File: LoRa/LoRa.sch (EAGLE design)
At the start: 9 parts, among them IC1 FT232RL, J1 UP2-AH-1-TH, U1 RFM69HCW, U3 AP2112K-3.3, X1 uFL/SMA

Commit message: Stuff
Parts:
- removed IC1: FT232RL, ftdichip:FT232RL
- added C10, C11: 20pF, SparkFun-Capacitors:4.7UF0603
- added C3, C5, C7: 1.0uF, SparkFun-Capacitors:1.0UF-0603-16V-10%
- added C4, C6: 0.1uF, SparkFun-Capacitors:0.1UF-0603-25V-(+80/-20%)
- added C8: 22uF, microbuilder:CAP_CERAMIC0805-NOOUTLINE
- added C9: 10uF, microbuilder:CAP_CERAMIC0805-NOOUTLINE
- added L1: 2.2uH/NRH2412T2R2MNGH, microbuilder:INDUCTORNRH2412T
- added R2, R3, R4, R6: 10k, SparkFun-Resistors:1KOHM-0603-1/10W-1%
- added SV2: (no value), con-lsta:FE05-1
- added U2: RFM69HCW, microbuilder:RFM69HCW_SMT
- added U4: BSS138, BSS138:BSS138
- added U5: LM3671MF-3.3/NOPB, microbuilder:VREG_LM3671
- added Y1: ECS-80-S-4X, ECS-80-S-4X:ECS-80-S-4X
- C1: value 10uF -> 0.1uF; device SparkFun-Capacitors:10UF-0603-6.3V-20% -> SparkFun-Capacitors:0.1UF-0603-25V-(+80/-20%)
- U1: value RFM69HCW -> STM32L053C8T6; device microbuilder:RFM69HCW_SMT -> STM32L053C8T6:STM32L053C8T6
- U3: value AP2112K-3.3 -> BSS138; device microbuilder:VREG_SOT23-5 -> BSS138:BSS138
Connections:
- removed net D_MINUS: J1.2
- removed net D_PLUS: J1.3
- removed net MISO: U1.MISO
- removed net MOSI: U1.MOSI
- removed net SCK: U1.SCK
- removed net VIN: C1.1, J1.1, R1.1, U3.IN
- new net 5V: C9.1, J1.1, R1.1, R3.1, R6.1, U5.VIN
- new net EN: R1.2, U5.EN
- new net NRST: SV2.1, U1.NRST
- new net OSC_IN: C11.1, U1.PH0-OSC_IN, Y1.2
- new net OSC_OUT: C10.1, U1.PH1-OSC_OUT, Y1.1
- new net SPI1_MISO: U1.PA6, U2.MISO
- new net SPI1_MOSI: U2.MOSI
- new net SPI1_SCK: U1.PA5, U2.SCK
- new net SPI_MOSI: U1.PA7
- new net SWCLK: SV2.4, U1.PA14
- new net SWDIO: SV2.2, U1.PA13
- new net USB_DM_3V3: R4.1, U1.PA11, U4.S
- new net USB_DM_5V: J1.2, R6.2, U4.D
- new net USB_DP_3V3: R2.1, U1.PA12, U3.S
- new net USB_DP_5V: J1.3, R3.2, U3.D
- net 3.3V: now also C1.1, C3.1, C4.1, C5.1, C6.1, C7.1, C8.1, L1.2, R2.2, R4.2, SV2.5, U1.VDDA, U1.VDD_USB, U2.VDD, U3.G, U4.G, U5.FB; no longer U3.OUT
- net CS: now also U2.NSS; no longer U1.NSS
- net DIO0: now also U2.DIO0; no longer U1.DIO0
- net DIO1: now also U2.DIO1; no longer U1.DIO1
- net DIO2: now also U2.DIO2; no longer U1.DIO2
- net DIO3: now also U2.DIO3; no longer U1.DIO3
- net DIO4: now also U2.DIO4; no longer U1.DIO4
- net DIO5: now also U2.DIO5; no longer U1.DIO5
- net GND: now also C10.2, C11.2, C3.2, C4.2, C5.2, C6.2, C7.2, C8.2, C9.2, SV2.3, U1.VSS, U1.VSSA, U2.GND@1, U2.GND@2, U2.GND@3, U5.GND; no longer U1.GND@1, U1.GND@2, U1.GND@3, U3.GND
- net N$1: now also U2.ANT; no longer U1.ANT
- net N$2: now also L1.1, U5.SW; no longer R1.2, U3.EN
- net RST: now also U2.RESET; no longer U1.RESET
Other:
- note added: "OSCILLATOR"
- note removed: "Linear Regulator"

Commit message: updates
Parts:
- added C12: UWD0J560MCL1GS, 56uF_Cap_6.3v:UWD0J560MCL1GS
- added C13, C16: 1.0uF, SparkFun-Capacitors:1.0UF-0603-16V-10%
- added C14, C15: 0.1uF, SparkFun-Capacitors:0.1UF-0603-25V-(+80/-20%)
- added C17: 4.7uF, SparkFun-Capacitors:4.7UF0603
- added R5: 1k, SparkFun-Resistors:1KOHM-0603-1/10W-1%
- added RESET: SWITCH, DiscreteComponents:SWITCH
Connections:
- new net +3V3: R5.2
- net 3.3V: now also C12.1, C13.1, C14.1, C15.1, C16.1
- net CS: now also U1.PA4
- net DIO0: now also U1.PB1
- net GND: now also C12.2, C13.2, C14.2, C15.2, C16.2, C17.2, RESET.P$1
- net NRST: now also C17.1, R5.1, RESET.P$2
- net RST: now also U1.PB0
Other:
- moved on the sheet: C1, C3, J1

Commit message: Finished Initial Routing
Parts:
- removed R2, R3, R4, R6: 10k, SparkFun-Resistors:1KOHM-0603-1/10W-1%
- removed U3, U4: BSS138, BSS138:BSS138
- added C18: 0.1uF, SparkFun-Capacitors:0.1UF-0603-25V-(+80/-20%)
- added CR1: USBLC6-2SC6, ESD_Protection:USBLC6-2SC6
- added J2, J3: (no value), SparkFun-Connectors:CONN_03
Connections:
- removed net +3V3: R5.2
- removed net SPI_MOSI: U1.PA7
- removed net USB_DM_5V: J1.2, R6.2, U4.D
- removed net USB_DP_5V: J1.3, R3.2, U3.D
- new net USB_DM: CR1.I/O2, J1.2
- new net USB_DP: CR1.I/O1, J1.3
- net 3.3V: now also C18.1, CR1.VBUS, J3.1, J3.2, J3.3, R5.2; no longer R2.2, R4.2, U3.G, U4.G
- net 5V: no longer R3.1, R6.1
- net GND: now also C18.2, CR1.GND, J2.1, J2.2, J2.3
- net SPI1_MOSI: now also U1.PA7
- net USB_DM_3V3: now also CR1.I/O2_2; no longer R4.1, U4.S
- net USB_DP_3V3: now also CR1.I/O1_2; no longer R2.1, U3.S
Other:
- note added: "ESD Protection"

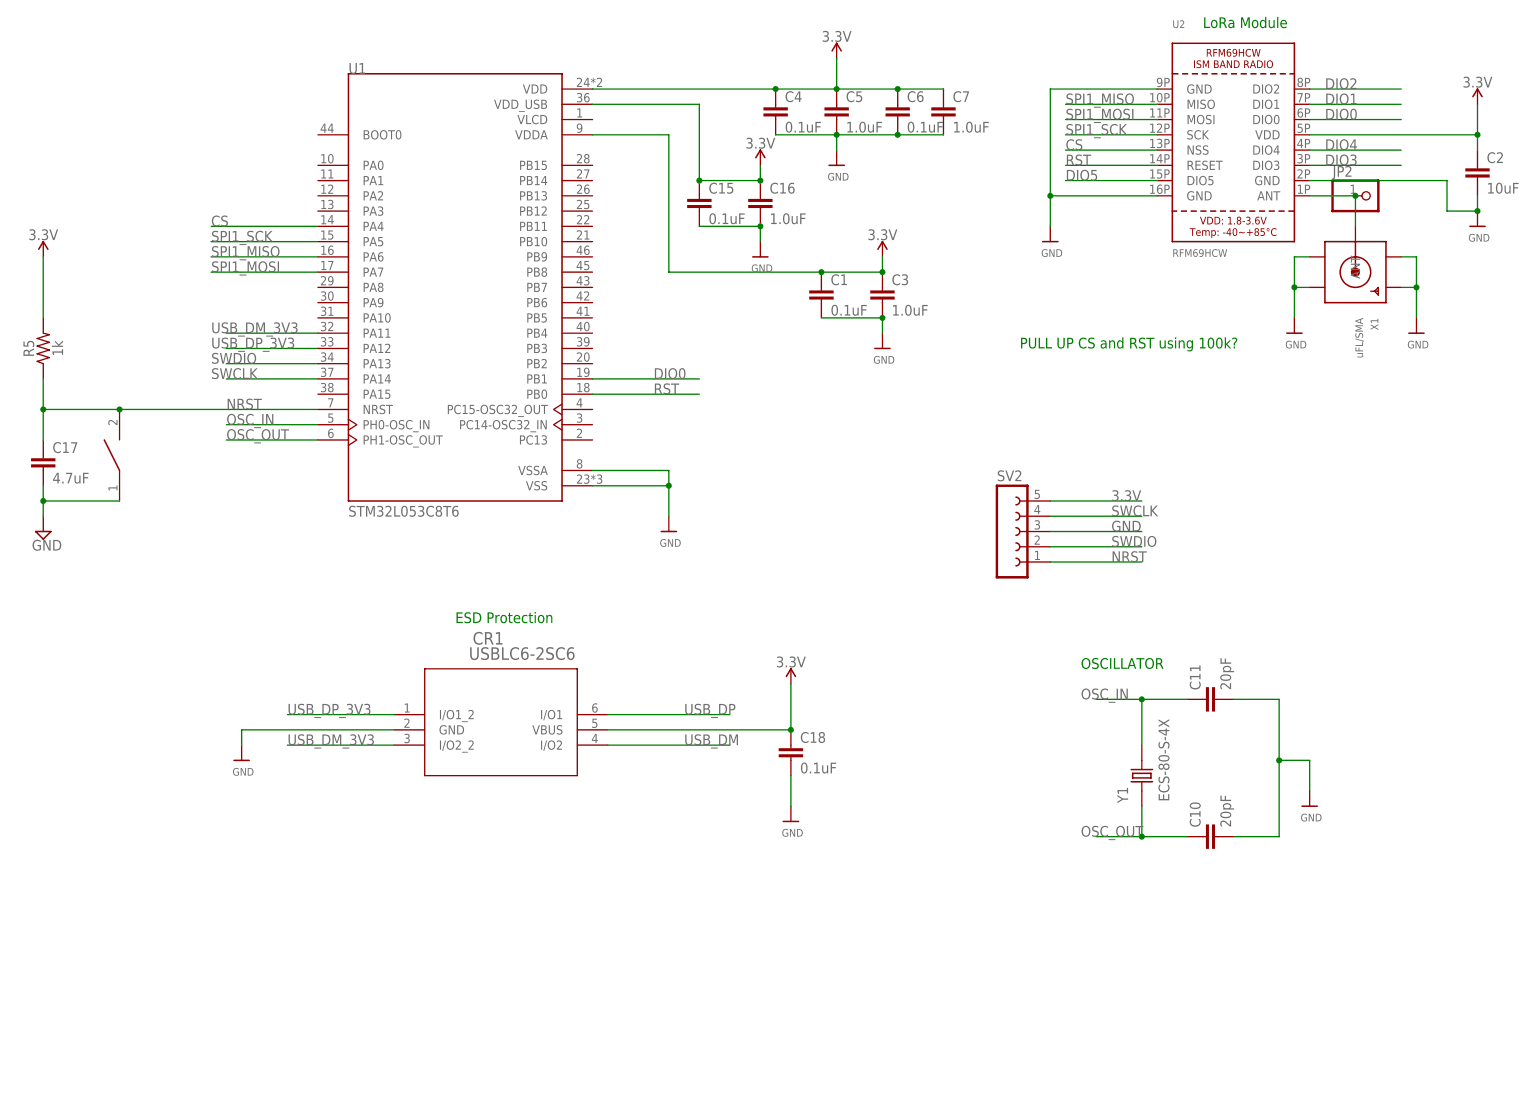
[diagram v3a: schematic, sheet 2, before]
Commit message: Added Labels to Schematic
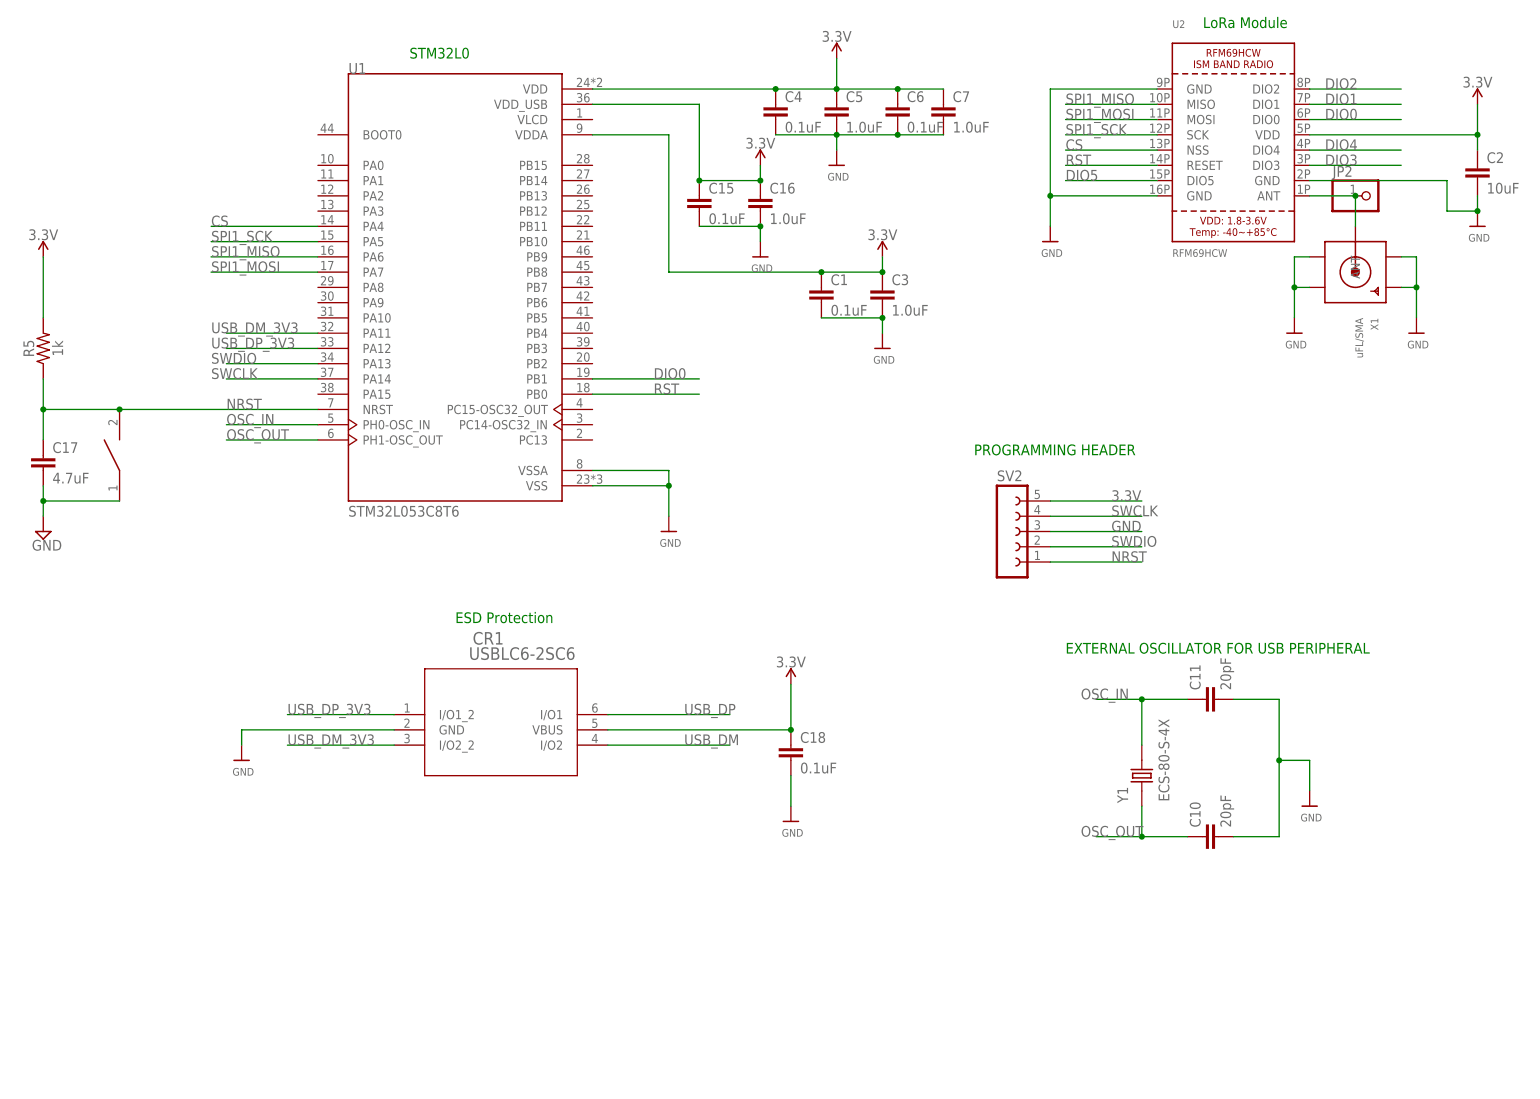
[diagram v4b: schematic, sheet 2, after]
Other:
- note added: "BUCK CONVERTER"
- note added: "CAPACITOR NETWORK FOR BUCK CONVERTER OUTPUT"
- note added: "EXTERNAL OSCILLATOR FOR USB PERIPHERAL"
- note added: "PROGRAMMING HEADER"
- note added: "STAR GROUND HEADERS"
- note added: "STM32L0"
- note added: "USB MALE CONNECTOR"
- note removed: "OSCILLATOR"
- note removed: "PULL UP CS and RST using 100k?"
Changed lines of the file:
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@@
 <sheets>
 <sheet>
-<description>Power and FTDI</description>
+<description>Power</description>
 <plain>
+<text x="55.88" y="218.44" size="1.778" layer="91">BUCK CONVERTER</text>
+<text x="142.24" y="210.82" size="1.778" layer="91">USB MALE CONNECTOR</text>
+<text x="48.26" y="165.1" size="1.778" layer="91">CAPACITOR NETWORK FOR BUCK CONVERTER OUTPUT</text>
+<text x="147.32" y="165.1" size="1.778" layer="91">STAR GROUND HEADERS</text>
 </plain>
 <instances>
@@
 <plain>
 <text x="205.74" y="228.6" size="1.778" layer="91">LoRa Module</text>
-<text x="175.26" y="175.26" size="1.778" layer="91">PULL UP CS and RST using 100k?</text>
-<text x="185.42" y="121.92" size="1.778" layer="91">OSCILLATOR</text>
+<text x="182.88" y="124.46" size="1.778" layer="91">EXTERNAL OSCILLATOR FOR USB PERIPHERAL</text>
 <text x="81.28" y="129.54" size="1.778" layer="91">ESD Protection</text>
+<text x="167.64" y="157.48" size="1.778" layer="91">PROGRAMMING HEADER</text>
+<text x="73.66" y="223.52" size="1.778" layer="91">STM32L0</text>
 </plain>
 <instances>

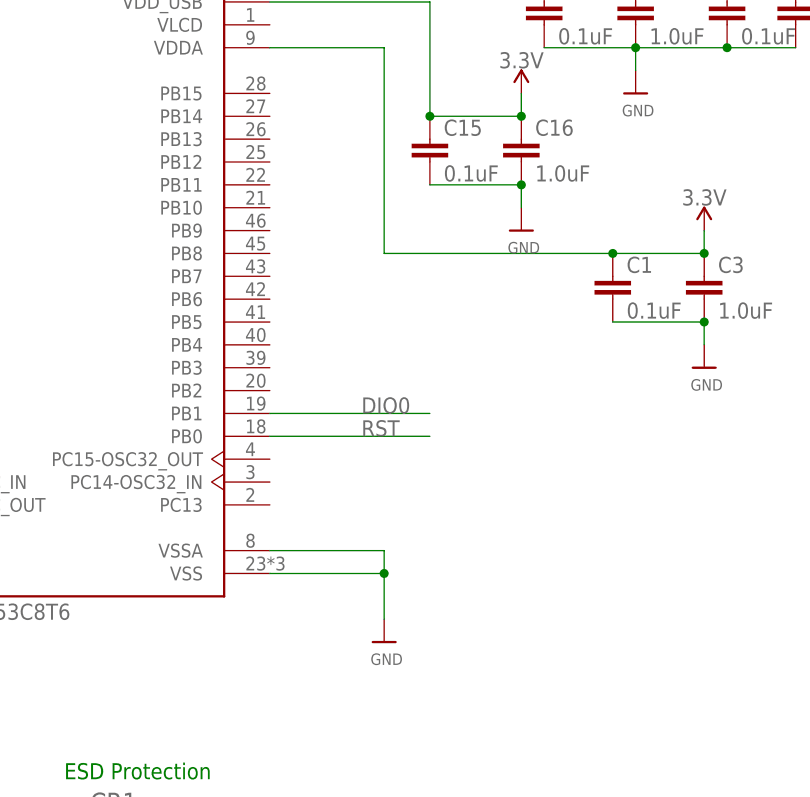
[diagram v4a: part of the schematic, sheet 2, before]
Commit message: added led indicator
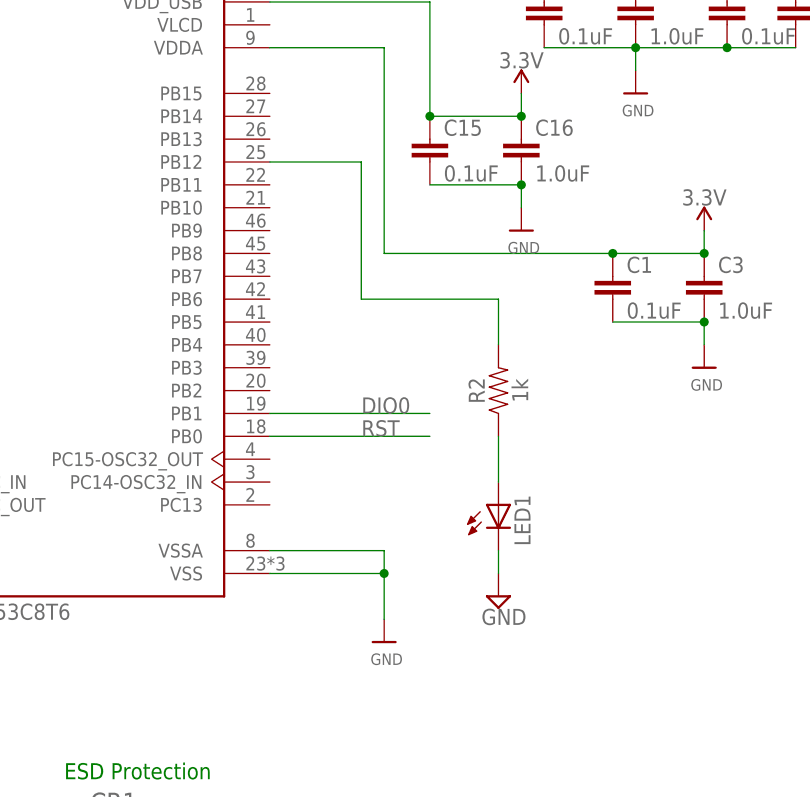
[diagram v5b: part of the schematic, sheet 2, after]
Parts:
- added LED1: (no value), led:LEDCHIP-LED0805
- added R2: 1k, SparkFun-Resistors:1KOHM-0603-1/10W-1%
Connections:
- new net N$3: R2.2, U1.PB12
- new net N$4: LED1.A, R2.1
- net GND: now also LED1.C
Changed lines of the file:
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@@
 <part name="J3" library="SparkFun-Connectors" library_urn="urn:adsk.eagle:library:513" deviceset="CONN_03" device="" package3d_urn="urn:adsk.eagle:package:38063/1"/>
 <part name="SUPPLY6" library="SparkFun-PowerSymbols" library_urn="urn:adsk.eagle:library:530" deviceset="3.3V" device=""/>
+<part name="LED1" library="led" library_urn="urn:adsk.eagle:library:259" deviceset="LED" device="CHIP-LED0805" package3d_urn="urn:adsk.eagle:package:15818/2">
+<attribute name="SPICEPREFIX" value="L"/>
+</part>
+<part name="GND1" library="supply2" library_urn="urn:adsk.eagle:library:372" deviceset="GND" device=""/>
+<part name="R2" library="SparkFun-Resistors" library_urn="urn:adsk.eagle:library:532" deviceset="1KOHM" device="-0603-1/10W-1%" package3d_urn="urn:adsk.eagle:package:39650/1" value="1k"/>
 </parts>
 <sheets>
@@
 <instance part="U$16" gate="G$1" x="45.72" y="106.68"/>
 <instance part="SUPPLY6" gate="G$1" x="12.7" y="190.5"/>
+<instance part="LED1" gate="G$1" x="129.54" y="160.02"/>
+<instance part="GND1" gate="GND" x="129.54" y="149.86">
+<attribute name="VALUE" x="127.635" y="146.685" size="1.778" layer="96"/>
+</instance>
+<instance part="R2" gate="G$1" x="129.54" y="172.72" rot="R90">
+<attribute name="NAME" x="128.016" y="172.72" size="1.778" layer="95" font="vector" rot="R90" align="bottom-center"/>
+<attribute name="VALUE" x="131.064" y="172.72" size="1.778" layer="96" font="vector" rot="R90" align="top-center"/>
+</instance>
 </instances>
 <busses>
@@
 <wire x1="71.12" y1="111.76" x2="45.72" y2="111.76" width="0.1524" layer="91"/>
 <wire x1="45.72" y1="111.76" x2="45.72" y2="109.22" width="0.1524" layer="91"/>
+</segment>
+<segment>
+<pinref part="LED1" gate="G$1" pin="C"/>
+<pinref part="GND1" gate="GND" pin="GND"/>
+<wire x1="129.54" y1="154.94" x2="129.54" y2="152.4" width="0.1524" layer="91"/>
 </segment>
 </net>
@@
 </segment>
 </net>
+<net name="N$3" class="0">
+<segment>
+<pinref part="U1" gate="G$1" pin="PB12"/>
+<wire x1="104.14" y1="198.12" x2="114.3" y2="198.12" width="0.1524" layer="91"/>
+<wire x1="114.3" y1="198.12" x2="114.3" y2="182.88" width="0.1524" layer="91"/>
+<wire x1="114.3" y1="182.88" x2="129.54" y2="182.88" width="0.1524" layer="91"/>
+<pinref part="R2" gate="G$1" pin="2"/>
+<wire x1="129.54" y1="177.8" x2="129.54" y2="182.88" width="0.1524" layer="91"/>
+</segment>
+</net>
+<net name="N$4" class="0">
+<segment>
+<pinref part="R2" gate="G$1" pin="1"/>
+<pinref part="LED1" gate="G$1" pin="A"/>
+<wire x1="129.54" y1="167.64" x2="129.54" y2="162.56" width="0.1524" layer="91"/>
+</segment>
+</net>

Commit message: Final touches
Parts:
- removed X1: uFL/SMA, microbuilder:SMACONNECTOR_EDGE_UFL
- added J4: EMPCB.SMAFSTJ.B.HT, EMPCB.SMAFSTJ.B.HT:EMPCB.SMAFSTJ.B.HT
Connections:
- net GND: now also J4.2; no longer X1.GND1, X1.GND2, X1.GND3, X1.GND4
- net N$1: now also J4.1; no longer X1.ANT
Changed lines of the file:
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@@
 <part name="U2" library="microbuilder" deviceset="RFM69HCW" device="_SMT" value="RFM69HCW"/>
 <part name="U$6" library="microbuilder" deviceset="GND" device=""/>
-<part name="X1" library="microbuilder" deviceset="SMACONNECTOR" device="_EDGE_UFL" value="uFL/SMA"/>
-<part name="U$7" library="microbuilder" deviceset="GND" device=""/>
-<part name="U$9" library="microbuilder" deviceset="GND" device=""/>
 <part name="JP2" library="microbuilder" deviceset="HEADER-1X1" device="ROUND"/>
 <part name="C2" library="SparkFun-Capacitors" library_urn="urn:adsk.eagle:library:510" deviceset="10UF" device="-0603-6.3V-20%" package3d_urn="urn:adsk.eagle:package:37414/1" value="10uF"/>
@@
 <part name="GND1" library="supply2" library_urn="urn:adsk.eagle:library:372" deviceset="GND" device=""/>
 <part name="R2" library="SparkFun-Resistors" library_urn="urn:adsk.eagle:library:532" deviceset="1KOHM" device="-0603-1/10W-1%" package3d_urn="urn:adsk.eagle:package:39650/1" value="1k"/>
+<part name="J4" library="EMPCB.SMAFSTJ.B.HT" deviceset="EMPCB.SMAFSTJ.B.HT" device=""/>
+<part name="U$17" library="microbuilder" deviceset="GND" device=""/>
 </parts>
 <sheets>
@@
 <instance part="U2" gate="G$1" x="210.82" y="210.82"/>
 <instance part="U$6" gate="G$1" x="251.46" y="195.58"/>
-<instance part="X1" gate="G$1" x="231.14" y="187.96" rot="R270"/>
-<instance part="U$7" gate="G$1" x="241.3" y="177.8"/>
-<instance part="U$9" gate="G$1" x="220.98" y="177.8"/>
 <instance part="JP2" gate="G$1" x="233.68" y="200.66"/>
 <instance part="C2" gate="G$1" x="251.46" y="203.2"/>
@@
 <attribute name="VALUE" x="131.064" y="172.72" size="1.778" layer="96" font="vector" rot="R90" align="top-center"/>
 </instance>
+<instance part="J4" gate="G$1" x="218.44" y="185.42"/>
+<instance part="U$17" gate="G$1" x="231.14" y="180.34"/>
 </instances>
 <busses>
@@
 <wire x1="251.46" y1="198.12" x2="251.46" y2="200.66" width="0.1524" layer="91"/>
 <junction x="251.46" y="198.12"/>
-</segment>
-<segment>
-<pinref part="X1" gate="G$1" pin="GND2"/>
-<pinref part="U$7" gate="G$1" pin="GND"/>
-<wire x1="238.76" y1="185.42" x2="241.3" y2="185.42" width="0.1524" layer="91"/>
-<wire x1="241.3" y1="185.42" x2="241.3" y2="180.34" width="0.1524" layer="91"/>
-<pinref part="X1" gate="G$1" pin="GND1"/>
-<wire x1="238.76" y1="190.5" x2="241.3" y2="190.5" width="0.1524" layer="91"/>
-<wire x1="241.3" y1="190.5" x2="241.3" y2="185.42" width="0.1524" layer="91"/>
-<junction x="241.3" y="185.42"/>
-</segment>
-<segment>
-<pinref part="X1" gate="G$1" pin="GND4"/>
-<pinref part="U$9" gate="G$1" pin="GND"/>
-<wire x1="223.52" y1="185.42" x2="220.98" y2="185.42" width="0.1524" layer="91"/>
-<wire x1="220.98" y1="185.42" x2="220.98" y2="180.34" width="0.1524" layer="91"/>
-<pinref part="X1" gate="G$1" pin="GND3"/>
-<wire x1="223.52" y1="190.5" x2="220.98" y2="190.5" width="0.1524" layer="91"/>
-<wire x1="220.98" y1="190.5" x2="220.98" y2="185.42" width="0.1524" layer="91"/>
-<junction x="220.98" y="185.42"/>
 </segment>
 <segment>
@@
 <pinref part="GND1" gate="GND" pin="GND"/>
 <wire x1="129.54" y1="154.94" x2="129.54" y2="152.4" width="0.1524" layer="91"/>
+</segment>
+<segment>
+<pinref part="J4" gate="G$1" pin="2"/>
+<wire x1="220.98" y1="185.42" x2="231.14" y2="185.42" width="0.1524" layer="91"/>
+<pinref part="U$17" gate="G$1" pin="GND"/>
+<wire x1="231.14" y1="182.88" x2="231.14" y2="185.42" width="0.1524" layer="91"/>
 </segment>
 </net>
@@
 <net name="N$1" class="0">
 <segment>
-<pinref part="X1" gate="G$1" pin="ANT"/>
 <wire x1="223.52" y1="200.66" x2="231.14" y2="200.66" width="0.1524" layer="91"/>
-<wire x1="231.14" y1="200.66" x2="231.14" y2="195.58" width="0.1524" layer="91"/>
 <pinref part="U2" gate="G$1" pin="ANT"/>
 <pinref part="JP2" gate="G$1" pin="1"/>
+<pinref part="J4" gate="G$1" pin="1"/>
+<wire x1="220.98" y1="187.96" x2="231.14" y2="187.96" width="0.1524" layer="91"/>
+<wire x1="231.14" y1="200.66" x2="231.14" y2="187.96" width="0.1524" layer="91"/>
 <junction x="231.14" y="200.66"/>
 </segment>
